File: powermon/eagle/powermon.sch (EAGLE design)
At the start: 42 parts, among them J1 USB, J2 USB, J3 TERMINAL-2, U1 LTC2943, U2 FT232RL, U3 LT1764AEQ, U4 ATMEGA328TQFP32

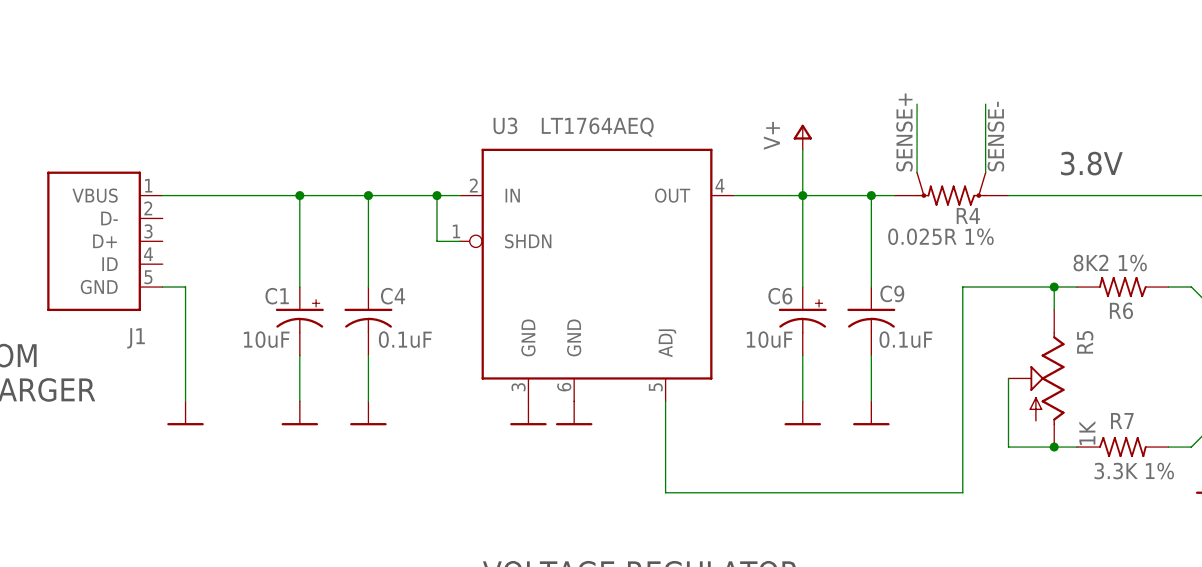
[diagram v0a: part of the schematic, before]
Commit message: Cleaned up the layout. Should be ready for final auto routing.
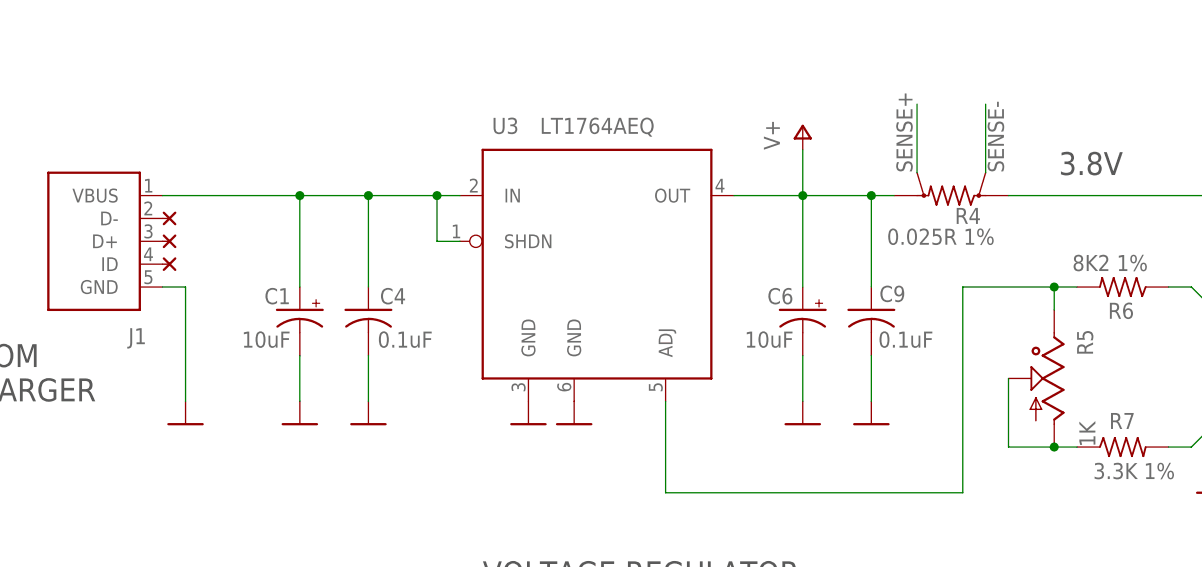
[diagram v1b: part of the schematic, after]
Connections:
- net N$18: now also R5.1, R5.2; no longer R5.A, R5.S
- net N$19: now also R5.3; no longer R5.E
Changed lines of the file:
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@@
 <part name="U$4" library="powermon" deviceset="NC" device=""/>
 <part name="U$6" library="powermon" deviceset="NC" device=""/>
+<part name="U$2" library="powermon" deviceset="NC" device=""/>
+<part name="U$7" library="powermon" deviceset="NC" device=""/>
+<part name="U$8" library="powermon" deviceset="NC" device=""/>
 </parts>
 <sheets>
@@
 <instance part="U$4" gate="G$1" x="68.58" y="53.34" rot="R180"/>
 <instance part="U$6" gate="G$1" x="68.58" y="50.8" rot="R180"/>
+<instance part="U$2" gate="G$1" x="2.54" y="208.28" rot="R180"/>
+<instance part="U$7" gate="G$1" x="2.54" y="205.74" rot="R180"/>
+<instance part="U$8" gate="G$1" x="2.54" y="203.2" rot="R180"/>
 </instances>
 <busses>
@@
 <pinref part="R6" gate="G$1" pin="2"/>
 <wire x1="104.14" y1="200.66" x2="101.6" y2="200.66" width="0.1524" layer="91"/>
-<pinref part="R5" gate="G$1" pin="E"/>
+<pinref part="R5" gate="G$1" pin="3"/>
 <wire x1="101.6" y1="200.66" x2="91.44" y2="200.66" width="0.1524" layer="91"/>
 <wire x1="101.6" y1="198.12" x2="101.6" y2="200.66" width="0.1524" layer="91"/>
@@
 <net name="N$18" class="0">
 <segment>
-<pinref part="R5" gate="G$1" pin="S"/>
+<pinref part="R5" gate="G$1" pin="2"/>
 <wire x1="96.52" y1="190.5" x2="96.52" y2="182.88" width="0.1524" layer="91"/>
 <pinref part="R7" gate="G$1" pin="1"/>
 <wire x1="104.14" y1="182.88" x2="101.6" y2="182.88" width="0.1524" layer="91"/>
-<pinref part="R5" gate="G$1" pin="A"/>
+<pinref part="R5" gate="G$1" pin="1"/>
 <junction x="101.6" y="182.88"/>
 <wire x1="101.6" y1="182.88" x2="96.52" y2="182.88" width="0.1524" layer="91"/>
